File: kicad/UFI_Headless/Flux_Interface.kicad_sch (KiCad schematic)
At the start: 12 parts, among them U6 SN74LS07D, U7 SN74LS07D, U8 74LVC14AD

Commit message: UFI Headless: 4-layer layout v0.1, LCSC sourcing, fab outputs
- build_pcb.py: footprints from the schematic netlist (KIID-linked), placement,
  pre-routed USB-C fan-out and MCU VSS stubs, In1 GND plane
- make_pcb.sh: Freerouting 2.4.1 routing, violation cleanup, supply widening,
  GND/3V3 pours, stitching vias; DRC 0 errors, schematic parity clean
- LCSC part numbers via JLCPCB API; crystal X322525MOB4SI (CL 12pF, 2x 18pF)
- fertigung/: Gerber, Excellon, BOM/CPL (KiCad + JLC format)

Co-Authored-By: Claude Opus 5.5 <noreply@anthropic.com>
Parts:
- C40, C41, C42: LCSC (none) -> C14663
- C43: LCSC (none) -> C15850
- RN1, RN2, RN3, RN4, RN5: LCSC (none) -> C20197
- U6, U7: LCSC (none) -> C371970; MPN SN74LS07D (alt. SN7407D) -> SN74LS07DR (alt. SN7407DR)
- U8: LCSC (none) -> C133541; MPN SN74LVC14AD -> SN74LVC14ADR

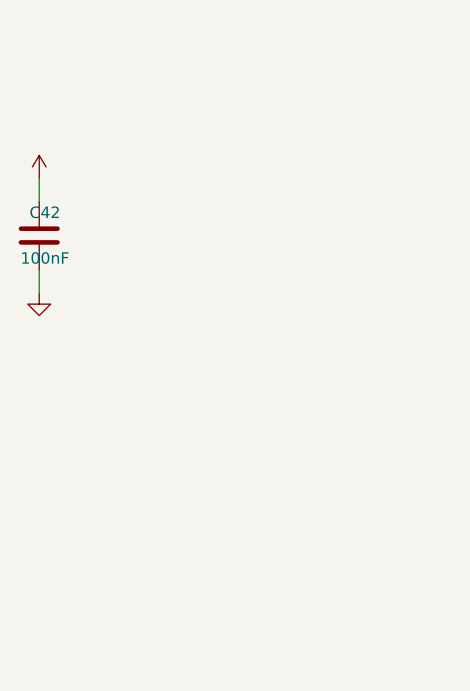
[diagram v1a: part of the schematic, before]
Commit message: UFI Headless v0.2: 8 MB PSRAM, ESD, drive polyfuses, test points
Schematic (new parts get fixed references above the v0.1 maxima, so all
existing references and PCB links stay unchanged):
- U11 APS6404L 8 MB QSPI PSRAM on OCTOSPIM P1 (PB2/PB10/PD11/PD12/PB13/
  PD13), C46, CE# pull-up R16
- D9-D11 ESDA6V1-5SC6 on the 13 Amiga J7 bus lines + MOTOR_A, D12 on IEC
- F2/F3 polyfuses: drive supplies FDD_5V/FDD_12V for J3 and J7 pins 12/23
- TP1-TP6 (3V3, 5V, 12V, GND, RDATA, INDEX), excluded from BOM/CPL
Layout (incremental ECO on the reviewed board):
- scripts/add_parts.py: re-net pads, collision-aware placement, rip up only
  what is in the way; make_pcb.sh 'eco' step
- fixes found on the way: supply pours ran after finish_pcb and left GND
  islands (LDO U4 ground!) without vias -> order swapped, GND pour check
  per net; island/dogbone vias never inside pads; manual_routes no longer
  re-applies the D+ fallback; pipeline filters robust against interleaved
  SWIG noise under pipefail
- DRC rule for the intentional J6/J7 silk overhang instead of warnings;
  netclasses cover the new drive supply nets
DRC: 0 errors, 0 warnings, 0 unconnected, parity clean, no via-in-pad.

Co-Authored-By: Claude Opus 5.5 <noreply@anthropic.com>
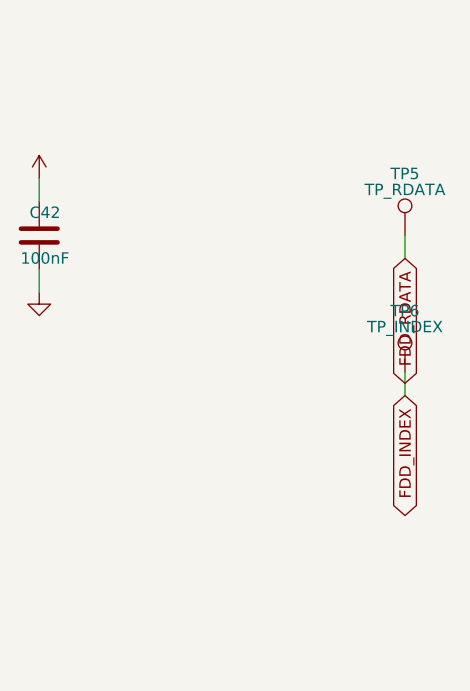
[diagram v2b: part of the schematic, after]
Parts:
- added TP5: TP_RDATA, TestPoint:TestPoint_Pad_D1.5mm, symbol Connector:TestPoint
- added TP6: TP_INDEX, TestPoint:TestPoint_Pad_D1.5mm, symbol Connector:TestPoint
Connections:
- net FDD_INDEX: now also TP6.1
- net FDD_RDATA: now also TP5.1
